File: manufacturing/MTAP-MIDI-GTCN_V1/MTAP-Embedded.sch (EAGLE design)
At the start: 32 parts, among them IC1 ESP32-WROOM-32UE-N8, IC2 AMS1117-3.3, J1 629105150521

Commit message: upd board
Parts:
- removed S3: (no value), switch_GruS:SLIDE_SW
- added S4: (no value), switch_GruS:452404020202
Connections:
- removed net GPIO26: IC1.IO26
- removed net GPIO27: IC1.IO27
- net EN: now also S2.P, S2.P1; no longer S2.S, S2.S1
- net PGND: now also S2.S, S2.S1; no longer S2.P, S2.P1
- net RXD: now also S4.COM; no longer S3A.P
- net RXD0: now also S4.4; no longer S3B.O
- net RXD1: now also IC1.IO27, S4.6; no longer S3B.S
- net TXD: now also S4.COM1; no longer S3B.P
- net TXD0: now also S4.1; no longer S3A.O
- net TXD1: now also IC1.IO26, S4.3; no longer S3A.S
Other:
- moved on the sheet: C1, C2, C6, C7, C8, C9, D1, D2, D3, D4, H1, IC2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

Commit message: adp adc #3 pcb
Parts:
- added D5: MCP33131-05-E, adc-dac_GruS:MCP33131-05-E
- added N1: TC2015, vreg_GruS:TC2015
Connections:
- new net +1V8: D5.AVDD, N1.VOUT
- new net ADI: D5.SDI
- new net AGND: D5.AIN-, D5.GND, N1.GND
- new net N$10: N1.BYP
- new net N$11: D5.AIN+
- new net N$6: D5.SDO
- new net N$7: D5.SCLK
- new net N$8: N1.!SHDN
- new net N$9: D5.VREF
- net +3V3: now also N1.VIN
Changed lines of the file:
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@@
 <part name="FRAMES3" library="frames_GruS" library_urn="urn:adsk.eagle:library:27468648" deviceset="HTL-A4H-V1" device=""/>
 <part name="S4" library="switch_GruS" library_urn="urn:adsk.eagle:library:13571161" deviceset="452404020202" device="" package3d_urn="urn:adsk.eagle:package:18255064/2"/>
+<part name="D5" library="adc-dac_GruS" library_urn="urn:adsk.eagle:library:27824108" deviceset="MCP33131-*" device="" package3d_urn="urn:adsk.eagle:package:38102767/2" technology="05-E"/>
+<part name="AGND1" library="supply_GruS" library_urn="urn:adsk.eagle:library:13579815" deviceset="AGND" device=""/>
+<part name="N1" library="vreg_GruS" library_urn="urn:adsk.eagle:library:13581047" deviceset="TC2*" device="" package3d_urn="urn:adsk.eagle:package:20920779/7" technology="015"/>
+<part name="AGND2" library="supply_GruS" library_urn="urn:adsk.eagle:library:13579815" deviceset="AGND" device=""/>
+<part name="+3V6" library="supply_GruS" library_urn="urn:adsk.eagle:library:13579815" deviceset="+3V3" device=""/>
+<part name="+3V7" library="supply_GruS" library_urn="urn:adsk.eagle:library:13579815" deviceset="+1V8" device=""/>
+<part name="+3V8" library="supply_GruS" library_urn="urn:adsk.eagle:library:13579815" deviceset="+1V8" device=""/>
 </parts>
 <sheets>
@@
 <attribute name="SHEET_HEADLINE" x="94.3" y="8.9" size="2.54" layer="94" font="vector" ratio="10" align="center"/>
 </instance>
+<instance part="D5" gate="G$1" x="73.66" y="203.2" smashed="yes">
+<attribute name="NAME" x="100.33" y="210.82" size="1.778" layer="95" align="center-left"/>
+<attribute name="VALUE" x="100.33" y="208.28" size="1.778" layer="96" align="center-left"/>
+</instance>
+<instance part="AGND1" gate="G$1" x="71.12" y="185.42" smashed="yes">
+<attribute name="VALUE" x="71.12" y="183.388" size="1.27" layer="96" font="vector" align="bottom-center"/>
+</instance>
+<instance part="N1" gate="G$1" x="81.28" y="157.48" smashed="yes">
+<attribute name="NAME" x="73.66" y="166.37" size="1.6764" layer="95" font="vector" ratio="10" align="bottom-center"/>
+<attribute name="VALUE" x="73.66" y="147.32" size="1.27" layer="96" font="vector" ratio="10" align="bottom-center"/>
+</instance>
+<instance part="AGND2" gate="G$1" x="66.04" y="147.32" smashed="yes">
+<attribute name="VALUE" x="66.04" y="145.288" size="1.27" layer="96" font="vector" align="bottom-center"/>
+</instance>
+<instance part="+3V6" gate="G$1" x="66.04" y="167.64" smashed="yes">
+<attribute name="VALUE" x="66.04" y="168.402" size="1.27" layer="96" font="vector" align="bottom-center"/>
+</instance>
+<instance part="+3V7" gate="G$1" x="99.06" y="167.64" smashed="yes">
+<attribute name="VALUE" x="99.06" y="168.402" size="1.27" layer="96" font="vector" align="bottom-center"/>
+</instance>
+<instance part="+3V8" gate="G$1" x="71.12" y="208.28" smashed="yes">
+<attribute name="VALUE" x="71.12" y="209.042" size="1.27" layer="96" font="vector" align="bottom-center"/>
+</instance>
 </instances>
 <busses>
 </busses>
 <nets>
+<net name="AGND" class="0">
+<segment>
+<pinref part="D5" gate="G$1" pin="AIN-"/>
+<wire x1="73.66" y1="195.58" x2="71.12" y2="195.58" width="0.1524" layer="91"/>
+<wire x1="71.12" y1="195.58" x2="71.12" y2="193.04" width="0.1524" layer="91"/>
+<pinref part="D5" gate="G$1" pin="GND"/>
+<wire x1="71.12" y1="193.04" x2="71.12" y2="187.96" width="0.1524" layer="91"/>
+<wire x1="73.66" y1="193.04" x2="71.12" y2="193.04" width="0.1524" layer="91"/>
+<junction x="71.12" y="193.04"/>
+<pinref part="AGND1" gate="G$1" pin="AGND"/>
+</segment>
+<segment>
+<wire x1="66.04" y1="157.48" x2="66.04" y2="149.86" width="0.1524" layer="91"/>
+<pinref part="AGND2" gate="G$1" pin="AGND"/>
+<pinref part="N1" gate="G$1" pin="GND"/>
+<wire x1="68.58" y1="157.48" x2="66.04" y2="157.48" width="0.1524" layer="91"/>
+</segment>
+</net>
+<net name="N$6" class="0">
+<segment>
+<pinref part="D5" gate="G$1" pin="SDO"/>
+<wire x1="104.14" y1="195.58" x2="106.68" y2="195.58" width="0.1524" layer="91"/>
+</segment>
+</net>
+<net name="N$7" class="0">
+<segment>
+<pinref part="D5" gate="G$1" pin="SCLK"/>
+<wire x1="104.14" y1="198.12" x2="106.68" y2="198.12" width="0.1524" layer="91"/>
+</segment>
+</net>
+<net name="ADI" class="0">
+<segment>
+<pinref part="D5" gate="G$1" pin="SDI"/>
+<wire x1="104.14" y1="200.66" x2="106.68" y2="200.66" width="0.1524" layer="91"/>
+</segment>
+</net>
+<net name="N$9" class="0">
+<segment>
+<pinref part="D5" gate="G$1" pin="VREF"/>
+<wire x1="73.66" y1="203.2" x2="68.58" y2="203.2" width="0.1524" layer="91"/>
+</segment>
+</net>
+<net name="N$11" class="0">
+<segment>
+<pinref part="D5" gate="G$1" pin="AIN+"/>
+<wire x1="73.66" y1="198.12" x2="68.58" y2="198.12" width="0.1524" layer="91"/>
+</segment>
+</net>
+<net name="+3V3" class="0">
+<segment>
+<pinref part="N1" gate="G$1" pin="VIN"/>
+<wire x1="68.58" y1="162.56" x2="66.04" y2="162.56" width="0.1524" layer="91"/>
+<wire x1="66.04" y1="162.56" x2="66.04" y2="165.1" width="0.1524" layer="91"/>
+<pinref part="+3V6" gate="G$1" pin="+3V3"/>
+</segment>
+</net>
+<net name="+1V8" class="0">
+<segment>
+<pinref part="N1" gate="G$1" pin="VOUT"/>
+<wire x1="96.52" y1="162.56" x2="99.06" y2="162.56" width="0.1524" layer="91"/>
+<pinref part="+3V7" gate="G$1" pin="+1V8"/>
+<wire x1="99.06" y1="162.56" x2="99.06" y2="165.1" width="0.1524" layer="91"/>
+</segment>
+<segment>
+<pinref part="D5" gate="G$1" pin="AVDD"/>
+<wire x1="73.66" y1="200.66" x2="71.12" y2="200.66" width="0.1524" layer="91"/>
+<wire x1="71.12" y1="200.66" x2="71.12" y2="205.74" width="0.1524" layer="91"/>
+<pinref part="+3V8" gate="G$1" pin="+1V8"/>
+</segment>
+</net>
+<net name="N$8" class="0">
+<segment>
+<pinref part="N1" gate="G$1" pin="!SHDN"/>
+<wire x1="68.58" y1="152.4" x2="63.5" y2="152.4" width="0.1524" layer="91"/>
+</segment>
+</net>
+<net name="N$10" class="0">
+<segment>
+<pinref part="N1" gate="G$1" pin="BYP"/>
+<wire x1="96.52" y1="152.4" x2="99.06" y2="152.4" width="0.1524" layer="91"/>
+</segment>
+</net>
 </nets>
 </sheet>

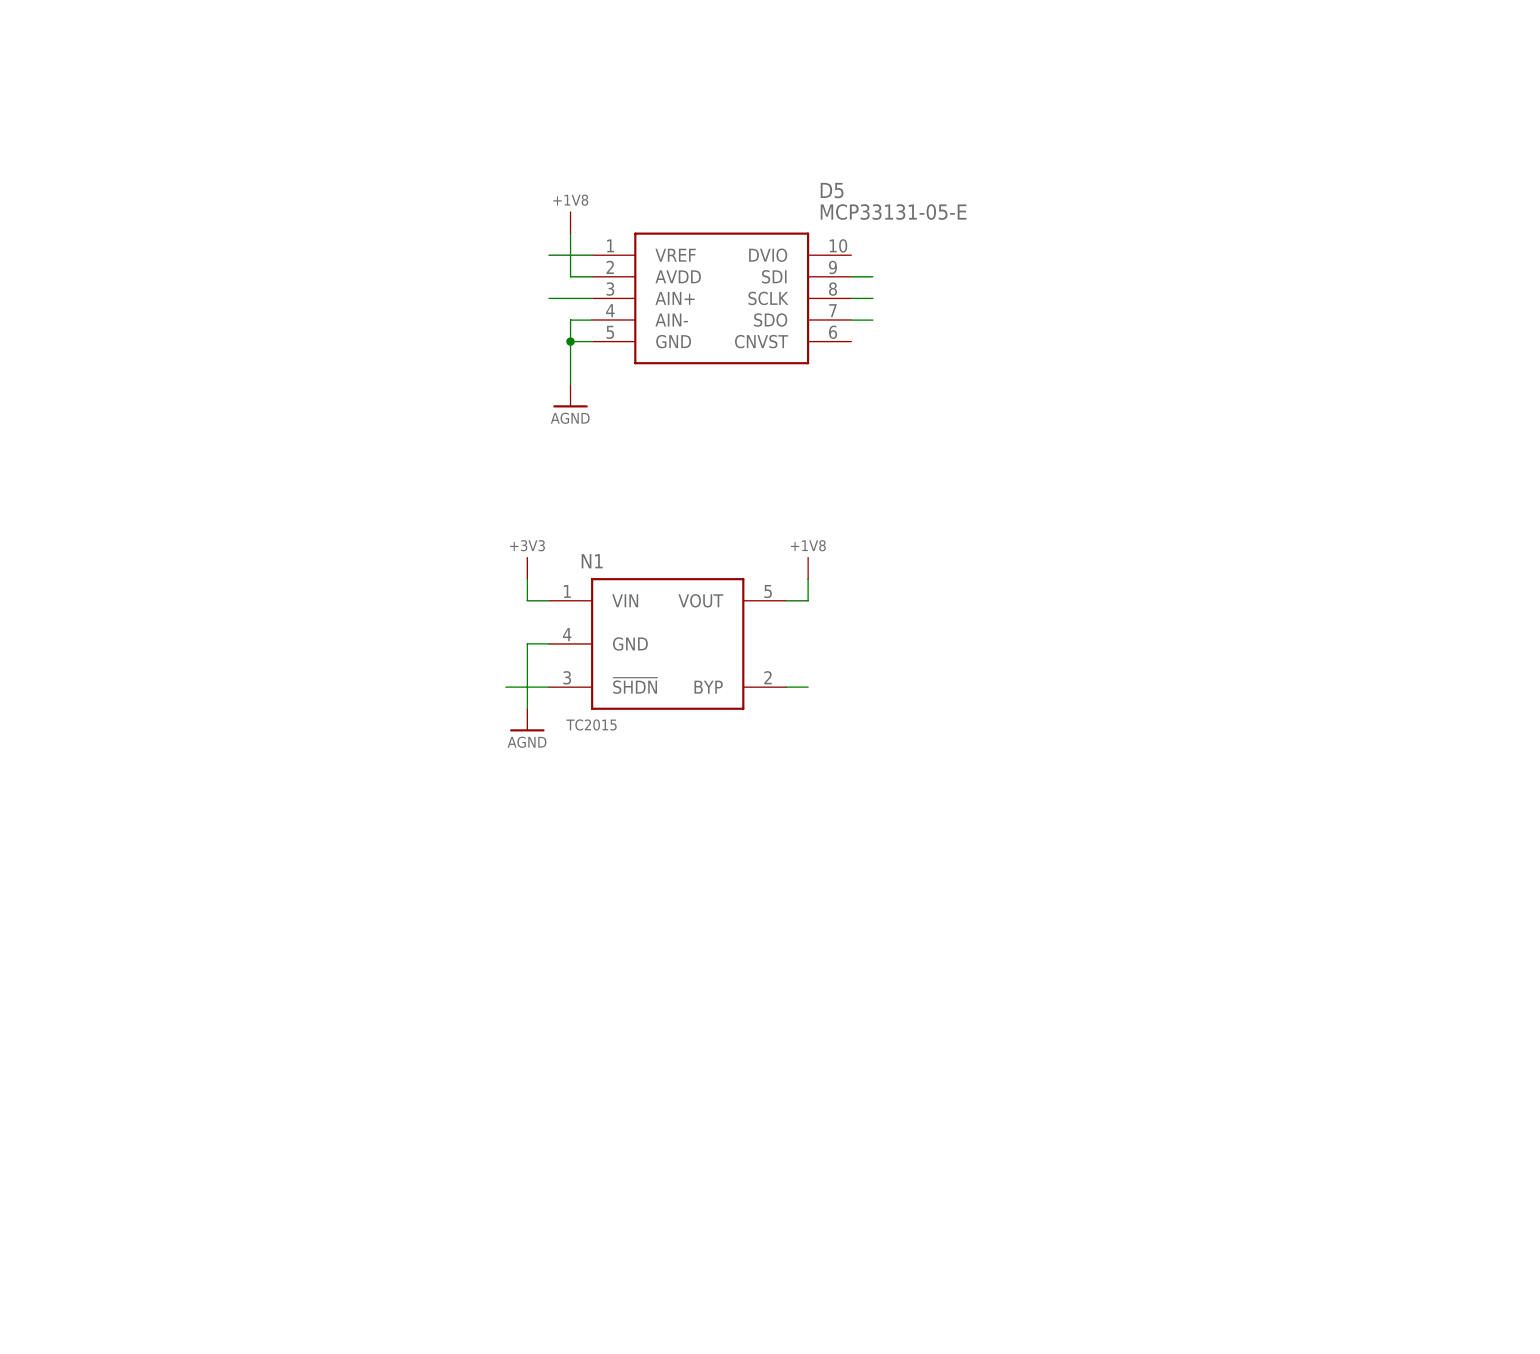
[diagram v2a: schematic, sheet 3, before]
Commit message: upd pcb analog
new filter
new ADC
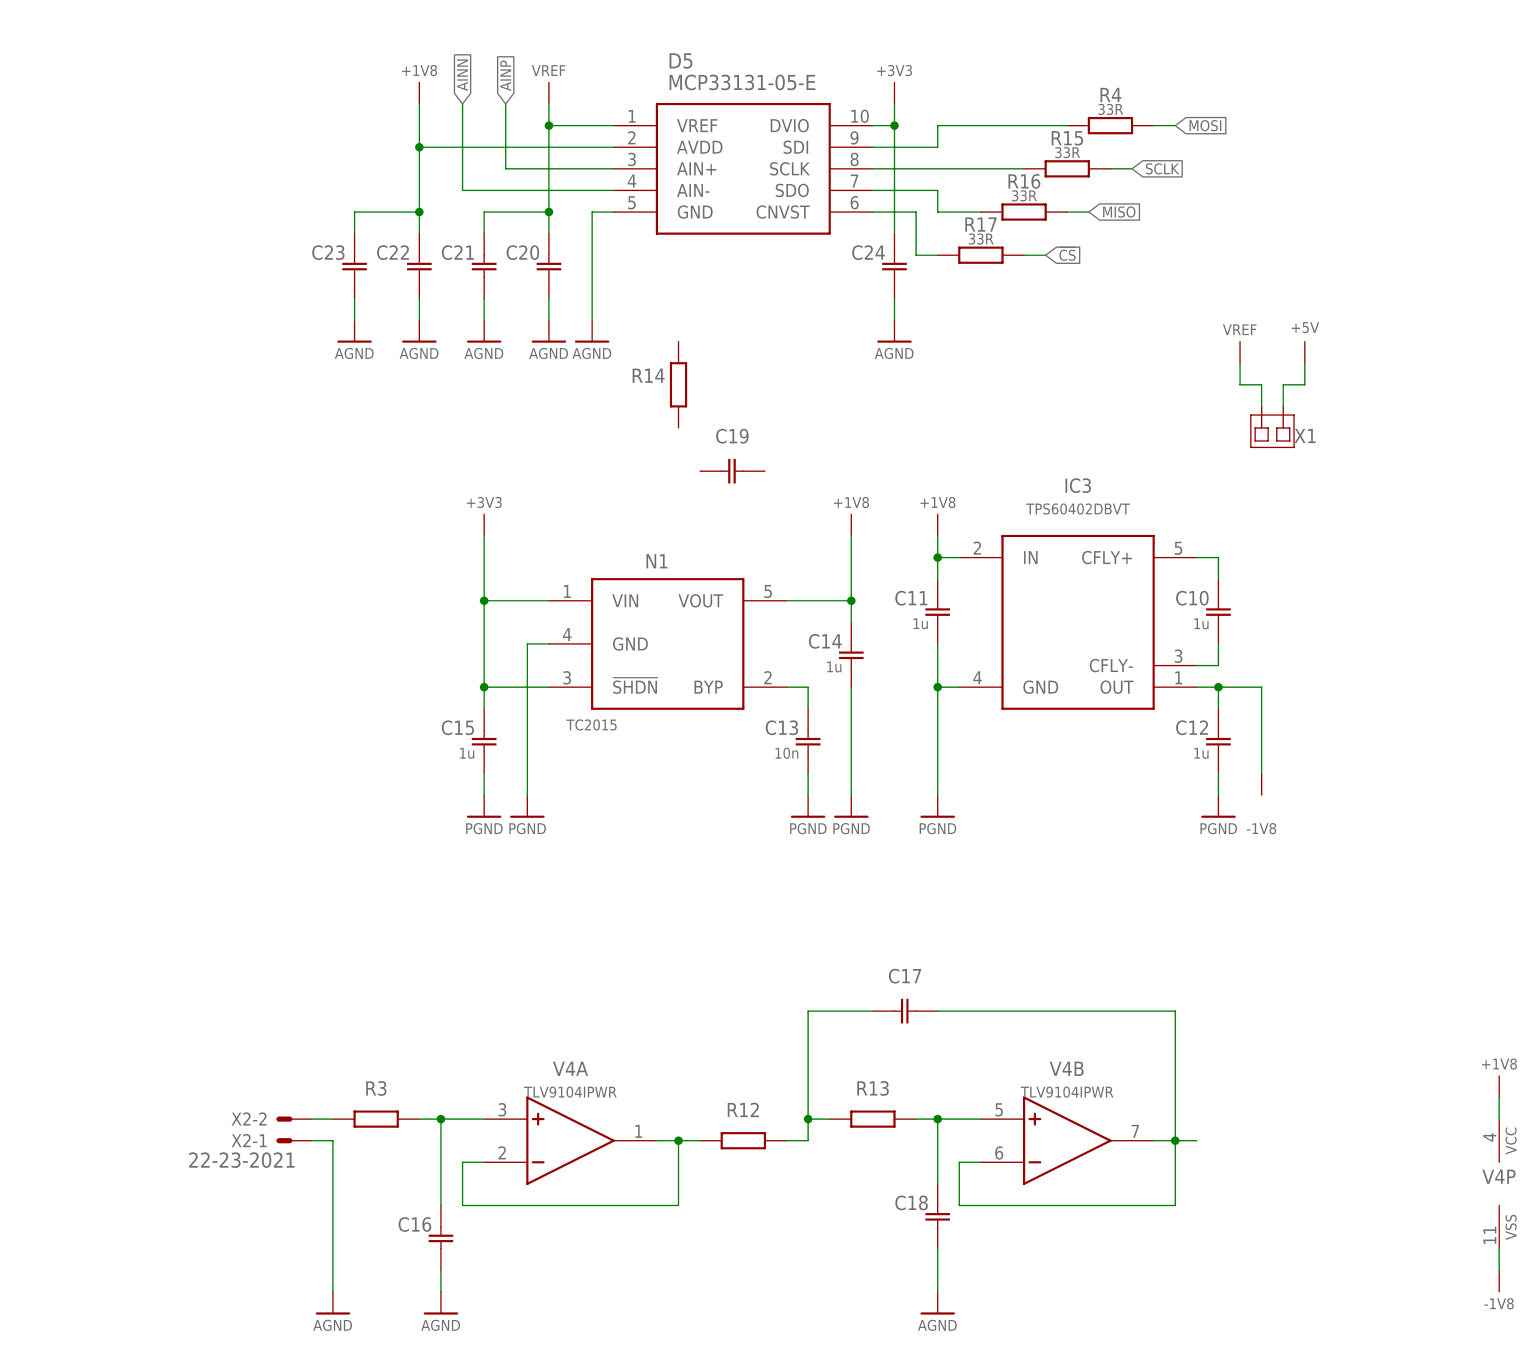
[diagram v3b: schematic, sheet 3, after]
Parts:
- added C10, C11, C12, C14, C15: 1u, rcl_GruS:C-EUC0805
- added C13: 10n, rcl_GruS:C-EUC0805
- added C16, C18, C20, C21, C22, C23, C24: (no value), rcl_GruS:C-EUC0805
- added C17, C19: (no value), rcl_GruS:C-EULC0805
- added IC3: TPS60402DBVT, vreg_GruS:TPS60402DBVT
- added R12, R13, R3: (no value), rcl_GruS:R-EU_R0805
- added R14: (no value), rcl_GruS:R-EUSR0805
- added R15, R16, R17, R4: 33R, rcl_GruS:R-EU_R0805
- added V4: TLV9104IPWR, opv_GruS:TLV9104IPWR
- added X1: (no value), con_GruS:JUMPSMD1FACH-1SHORT
- added X2: 22-23-2021, con-molex:22-23-2021
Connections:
- net N$11 renamed AINP
- removed net ADI: D5.SDI
- new net !CS: R17.2
- new net -1V8: C12.1, IC3.OUT, V4P.VSS
- new net AINN: D5.AIN-
- new net MISO: R16.2
- new net MOSI: R4.2
- new net N$11: D5.SDO, R16.1
- new net N$12: C18.1, R13.2, V4B.P
- new net N$13: C17.1, V4B.N, V4B.O
- new net N$14: D5.SCLK, R15.1
- new net N$17: C10.2, IC3.CFLY-
- new net N$18: C10.1, IC3.CFLY+
- new net N$19: D5.SDI, R4.1
- new net N$5: D5.CNVST, R17.1
- new net SCLK: R15.2
- new net VREF: C20.1, C21.1, D5.VREF, X1.2
- net +1V8: now also C11.1, C14.1, C22.1, C23.1, IC3.IN, V4P.VCC
- net +3V3: now also C15.1, C24.1, D5.DVIO, N1.!SHDN
- net +5V: now also X1.1
- net AGND: now also C16.2, C18.2, C20.2, C21.2, C22.2, C23.2, C24.2, X2-1.S; no longer D5.AIN-, N1.GND
- net N$10: now also C13.1
- net N$6: now also R12.1, V4A.N, V4A.O; no longer D5.SDO
- net N$7: now also C16.1, R3.2, V4A.P; no longer D5.SCLK
- net N$8: now also R3.1, X2-2.S; no longer N1.!SHDN
- net N$9: now also C17.2, R12.2, R13.1; no longer D5.VREF
- net PGND: now also C11.2, C12.2, C13.2, C14.2, C15.2, IC3.GND, N1.GND
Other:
- moved on the sheet: D5

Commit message: upd analog
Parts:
- removed C19: (no value), rcl_GruS:C-EULC0805
- removed R14: (no value), rcl_GruS:R-EUSR0805
- C16: value (none) -> 10n
- C17: value (none) -> 180n
- C18: value (none) -> 10nF
- C20, C22: value (none) -> 100n
- C21, C23: value (none) -> 1u
- R12: value (none) -> 560R
- R13: value (none) -> 1k
- R3: value (none) -> 6k2
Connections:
- removed net N$13: C17.1, V4B.N, V4B.O
- net AINP: now also C17.1, V4B.N, V4B.O
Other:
- moved on the sheet: C16, C17, C18, R13
